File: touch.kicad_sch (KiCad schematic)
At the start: 4 parts, among them J3 Touch_Top, J4 Touch_Top, U7 MTCH2120-V/REB, U8 MTCH2120-V/REB

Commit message: save progress before refactor
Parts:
- added R13, R14, R15, R16, R17, R18, R19, R20, R21, R22, R23, R24, R25, R26, R27, R28, R29, R30, R31, R32, R33, R34, R35, R36: 100k, Resistor_SMD:R_0402_1005Metric, symbol Device:R_Small
- J3: now left out of the parts list
- J4: value Touch_Top -> Touch_Btm; now left out of the parts list
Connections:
- net at U8.10 (BUTTON5/GPIO5): now also R18.2
- net at U8.13 (BUTTON6/GPIO6): now also R19.1
- net at U8.14 (BUTTON7/GPIO7): now also R20.1
- net at U8.15 (BUTTON8/GPIO8): now also R21.1
- net at U8.16 (BUTTON9/GPIO9): now also R22.1
- net at U8.17 (BUTTON10/GPIO10): now also R23.1
- net at U8.18 (BUTTON11/DS/GPIO11): now also R24.1
- net at U8.5 (BUTTON0/GPIO0): now also R13.2
- net at U8.6 (BUTTON1/GPIO1): now also R14.2
- net at U8.7 (BUTTON2/GPIO2): now also R15.2
- net at U8.8 (BUTTON3/GPIO3): now also R16.2
- net at U8.9 (BUTTON4/GPIO4): now also R17.2
- net TOUCH_BTM_1: now reaches J4.1 (Pin_1)
- net TOUCH_BTM_1: now also R13.1
- net TOUCH_BTM_10: now reaches J4.10 (Pin_10)
- net TOUCH_BTM_10: now also R22.2
- net TOUCH_BTM_11: now reaches J4.11 (Pin_11)
- net TOUCH_BTM_11: now also R23.2
- net TOUCH_BTM_12: now reaches J4.12 (Pin_12)
- net TOUCH_BTM_12: now also R24.2
- net TOUCH_BTM_2: now reaches J4.2 (Pin_2)
- net TOUCH_BTM_2: now also R14.1
- net TOUCH_BTM_3: now reaches J4.3 (Pin_3)
- net TOUCH_BTM_3: now also R15.1
- net TOUCH_BTM_4: now reaches J4.4 (Pin_4)
- net TOUCH_BTM_4: now also R16.1
- net TOUCH_BTM_5: now reaches J4.5 (Pin_5)
- net TOUCH_BTM_5: now also R17.1
- net TOUCH_BTM_6: now reaches J4.6 (Pin_6)
- net TOUCH_BTM_6: now also R18.1
- net TOUCH_BTM_7: now reaches J4.7 (Pin_7)
- net TOUCH_BTM_7: now also R19.2
- net TOUCH_BTM_8: now reaches J4.8 (Pin_8)
- net TOUCH_BTM_8: now also R20.2
- net TOUCH_BTM_9: now reaches J4.9 (Pin_9)
- net TOUCH_BTM_9: now also R21.2
- net at U7.10 (BUTTON5/GPIO5): now also R30.2
- net at U7.13 (BUTTON6/GPIO6): now also R36.1
- net at U7.14 (BUTTON7/GPIO7): now also R35.1
- net at U7.15 (BUTTON8/GPIO8): now also R34.1
- net at U7.16 (BUTTON9/GPIO9): now also R33.1
- net at U7.17 (BUTTON10/GPIO10): now also R32.1
- net at U7.18 (BUTTON11/DS/GPIO11): now also R31.1
- net GND: now reaches U7.2 (ADD_SEL)
- net at U7.5 (BUTTON0/GPIO0): now also R25.2
- net at U7.6 (BUTTON1/GPIO1): now also R26.2
- net at U7.7 (BUTTON2/GPIO2): now also R27.2
- net at U7.8 (BUTTON3/GPIO3): now also R28.2
- net at U7.9 (BUTTON4/GPIO4): now also R29.2
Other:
- moved on the sheet: J4

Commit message: progress dump
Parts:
- added C35, C37: 100nF, symbol Device:C_Small
- added C36, C38: 2.2uF, symbol Device:C_Small
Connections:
- net GND: now also U7.12 (GPIO12), U7.21 (EPAD), U7.3 (GND), U8.12 (GPIO12), U8.21 (EPAD), U8.3 (GND), C35.2, C36.2, C37.2, C38.2
- net TOUCH_TOP_4: now reaches R28.1
- net TOUCH_TOP_4: now also J3.4 (Pin_4)
- net TOUCH_TOP_3: now reaches R27.1
- net TOUCH_TOP_3: now also J3.3 (Pin_3)
- net SCL_G1: now reaches U8.1 (SCL)
- net SCL_G1: now also U7.1 (SCL)
- net TOUCH_INT: now reaches U8.11 (INT*)
- net TOUCH_INT: now also U7.11 (INT*)
- net TOUCH_RST: now reaches U8.19 (RESET*)
- net TOUCH_RST: now also U7.19 (RESET*)
- net +3V3_G1: now reaches U8.2 (ADD_SEL)
- net +3V3_G1: now also U7.4 (VDD), U8.4 (VDD), C35.1, C36.1, C37.1, C38.1
- net SDA_G1: now reaches U8.20 (SDA)
- net SDA_G1: now also U7.20 (SDA)
- net TOUCH_TOP_6: now reaches R30.1
- net TOUCH_TOP_6: now also J3.6 (Pin_6)
- net TOUCH_TOP_8: now reaches R35.2
- net TOUCH_TOP_8: now also J3.8 (Pin_8)
- net TOUCH_TOP_1: now reaches J3.1 (Pin_1)
- net TOUCH_TOP_1: now also R25.1
- net TOUCH_TOP_10: now reaches J3.10 (Pin_10)
- net TOUCH_TOP_10: now also R33.2
- net TOUCH_TOP_11: now reaches J3.11 (Pin_11)
- net TOUCH_TOP_11: now also R32.2
- net TOUCH_TOP_12: now reaches J3.12 (Pin_12)
- net TOUCH_TOP_12: now also R31.2
- net TOUCH_TOP_2: now reaches J3.2 (Pin_2)
- net TOUCH_TOP_2: now also R26.1
- net TOUCH_TOP_5: now reaches J3.5 (Pin_5)
- net TOUCH_TOP_5: now also R29.1
- net TOUCH_TOP_7: now reaches J3.7 (Pin_7)
- net TOUCH_TOP_7: now also R36.2
- net TOUCH_TOP_9: now reaches J3.9 (Pin_9)
- net TOUCH_TOP_9: now also R34.2
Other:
- moved on the sheet: J3

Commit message: finish up everything but nfc
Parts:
- C35, C37: footprint (none) -> Capacitor_SMD:C_0402_1005Metric; LCSC Part (none) -> C1525
- C36, C38: footprint (none) -> Capacitor_SMD:C_0402_1005Metric; LCSC Part (none) -> C12530
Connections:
- net +3V3_G1 renamed +3V3_G2
- net SCL_G1 renamed SCL_G2
- net SDA_G1 renamed SDA_G2

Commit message: progress
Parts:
- removed J3: Touch_Top, custom_footprints:Touch_Surface_12_Pad, symbol Connector_Generic:Conn_01x12
- removed J4: Touch_Btm, custom_footprints:Touch_Surface_12_Pad, symbol Connector_Generic:Conn_01x12
- removed R15, R16, R17, R18, R19, R20, R21, R22, R23, R24, R25, R26, R27, R28, R29, R30, R31, R32, R33, R34, R35, R36: 100k, Resistor_SMD:R_0402_1005Metric, symbol Device:R_Small
- removed U7, U8: MTCH2120-V/REB, MTCH2120:QFN_MTCH2120-V&slash_REB_MCH, symbol MTCH2120:MTCH2120-V_REB
- added R10, R9: 4.7k, symbol Device:R_Small
- added U7, U8: CAP1208-1-A4-TR, QFN16_3x3MC_MCH, symbol CAP1208-1-A4-TR:CAP1208-1-A4-TR
- C35, C37: footprint Capacitor_SMD:C_0402_1005Metric -> (none); LCSC Part C1525 -> (none)
- C36, C38: value 2.2uF -> 1uF; footprint Capacitor_SMD:C_0402_1005Metric -> (none); LCSC Part C12530 -> (none)
- R13, R14: value 100k -> 4.7k; footprint Resistor_SMD:R_0402_1005Metric -> (none); LCSC Part C25741 -> (none)
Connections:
- net TOUCH_BTM_1 is gone; now on net +3V3_G2: R13.1
- net TOUCH_BTM_2 is gone; now on net +3V3_G2: R14.1
- net +3V3_G2: now also R10.1, R9.1, U7.4 (VDD), U8.4 (VDD)
- net GND: now also U7.17 (EPAD), U7.7 (GND), U7.8 (GND), U8.17 (EPAD), U8.7 (GND), U8.8 (GND)
- net TOUCH_INT: now also U7.1 (*ALERT), U8.1 (*ALERT)
- net SDA_T2: now reaches R13.2
- net SDA_T2: now also U8.2 (SMDATA)
- net SCL_T2: now reaches R14.2
- net SCL_T2: now also U8.3 (SMCLK)
- new net SCL_T1: R10.2, U7.3 (SMCLK)
- new net SDA_T1: R9.2, U7.2 (SMDATA)

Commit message: push changes before removing fuel gauge
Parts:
- added J3: Touch_Surface_Top, custom_footprints:Touch_Surface_8_Pad, symbol Connector_Generic:Conn_01x08
- added J4: Touch_Surface_Bottom, custom_footprints:Touch_Surface_8_Pad, symbol Connector_Generic:Conn_01x08
- C35, C37: footprint (none) -> Capacitor_SMD:C_0402_1005Metric; LCSC Part (none) -> C1525
- C36, C38: footprint (none) -> Capacitor_SMD:C_0402_1005Metric; LCSC Part (none) -> C52923
- R10, R13, R14, R9: footprint (none) -> Resistor_SMD:R_0402_1005Metric; LCSC Part (none) -> C25900
- U7, U8: LCSC Part (none) -> C2652055; now left out of the parts list
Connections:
- net at U7.10 (CS7): now also J3.7 (Pin_7)
- net at U7.11 (CS6): now also J3.6 (Pin_6)
- net at U7.12 (CS5): now also J3.5 (Pin_5)
- net at U7.13 (CS4): now also J3.4 (Pin_4)
- net at U7.14 (CS3): now also J3.3 (Pin_3)
- net at U7.15 (CS2): now also J3.2 (Pin_2)
- net at U7.16 (CS1): now also J3.1 (Pin_1)
- net at U7.9 (CS8): now also J3.8 (Pin_8)
- net at U8.10 (CS7): now also J4.7 (Pin_7)
- net at U8.11 (CS6): now also J4.6 (Pin_6)
- net at U8.12 (CS5): now also J4.5 (Pin_5)
- net at U8.13 (CS4): now also J4.4 (Pin_4)
- net at U8.14 (CS3): now also J4.3 (Pin_3)
- net at U8.15 (CS2): now also J4.2 (Pin_2)
- net at U8.16 (CS1): now also J4.1 (Pin_1)
- net at U8.9 (CS8): now also J4.8 (Pin_8)

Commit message: hopefully final schematic before splitting out
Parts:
- J3, J4: now left out of the parts list
- U6: renamed from U7; now in the parts list
- U7: renamed from U8; now in the parts list
- renumbered C35 to C22, C37 to C23, C36 to C24, C38 to C25, R9 to R10, R13 to R11, R10 to R12, R14 to R13
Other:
- moved on the sheet: C22, C23, C24, C25, J3, J4, R10, R11, R12, R13, U6, U7

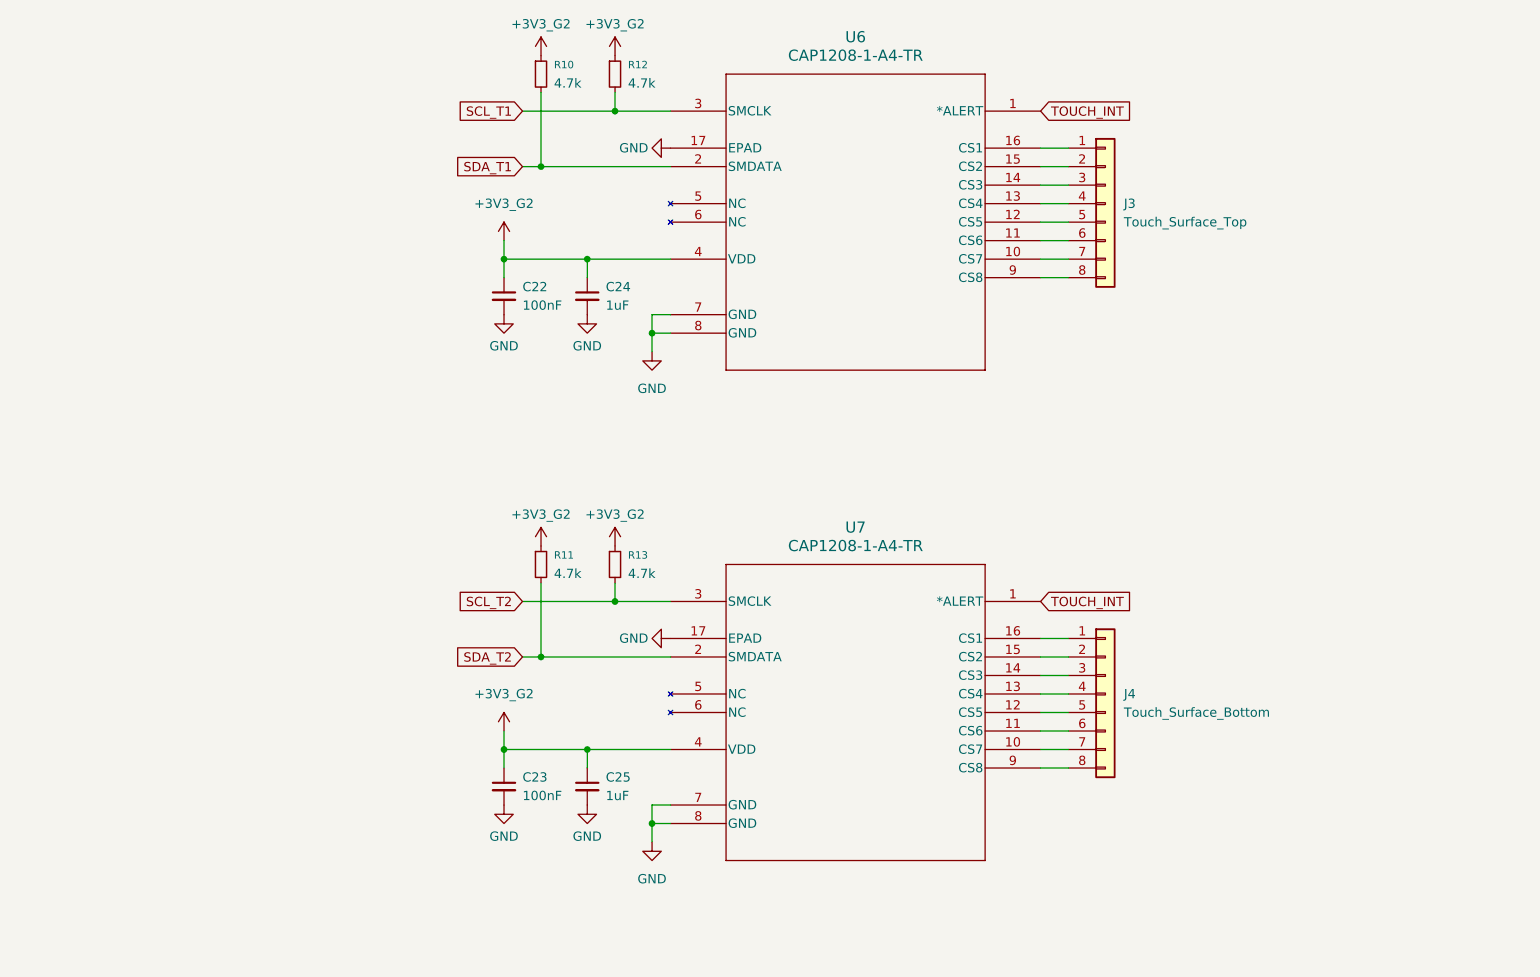
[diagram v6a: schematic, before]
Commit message: prepare schematic for devboard
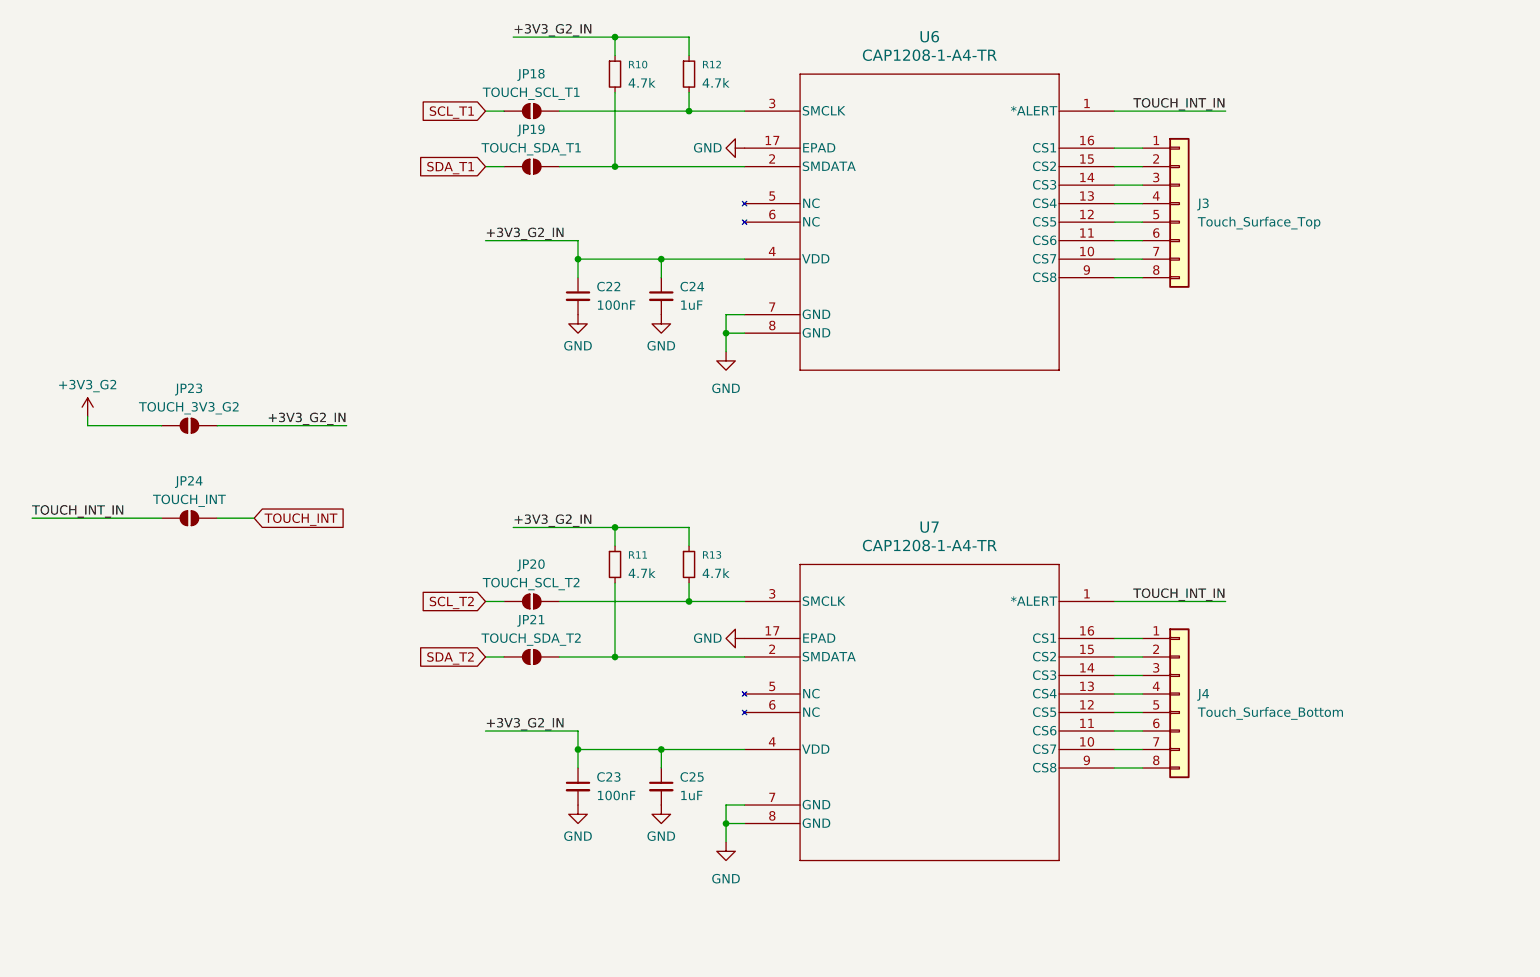
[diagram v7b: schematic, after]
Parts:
- added JP18: TOUCH_SCL_T1, Jumper:SolderJumper-2_P1.3mm_Open_Pad1.0x1.5mm, symbol Jumper:SolderJumper_2_Open
- added JP19: TOUCH_SDA_T1, Jumper:SolderJumper-2_P1.3mm_Open_Pad1.0x1.5mm, symbol Jumper:SolderJumper_2_Open
- added JP20: TOUCH_SCL_T2, Jumper:SolderJumper-2_P1.3mm_Open_Pad1.0x1.5mm, symbol Jumper:SolderJumper_2_Open
- added JP21: TOUCH_SDA_T2, Jumper:SolderJumper-2_P1.3mm_Open_Pad1.0x1.5mm, symbol Jumper:SolderJumper_2_Open
- added JP23: TOUCH_3V3_G2, Jumper:SolderJumper-2_P1.3mm_Open_Pad1.0x1.5mm, symbol Jumper:SolderJumper_2_Open
- added JP24: TOUCH_INT, Jumper:SolderJumper-2_P1.3mm_Open_Pad1.0x1.5mm, symbol Jumper:SolderJumper_2_Open
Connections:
- net +3V3_G2: now also JP23.1 (A); no longer C22.1, C23.1, C24.1, C25.1, R10.1, R11.1, R12.1, R13.1, U6.4 (VDD), U7.4 (VDD)
- net SCL_T1: now also JP18.1 (A); no longer R12.2, U6.3 (SMCLK)
- net SCL_T2: now also JP20.1 (A); no longer R13.2, U7.3 (SMCLK)
- net SDA_T1: now also JP19.1 (A); no longer R10.2, U6.2 (SMDATA)
- net SDA_T2: now also JP21.1 (A); no longer R11.2, U7.2 (SMDATA)
- net TOUCH_INT: now also JP24.2 (B); no longer U6.1 (*ALERT), U7.1 (*ALERT)
- new net: JP21.2 (B), R11.2, U7.2 (SMDATA)
- new net: JP19.2 (B), R10.2, U6.2 (SMDATA)
- new net: JP18.2 (B), R12.2, U6.3 (SMCLK)
- new net: JP20.2 (B), R13.2, U7.3 (SMCLK)
- new net +3V3_G2_IN: C22.1, C23.1, C24.1, C25.1, JP23.2 (B), R10.1, R11.1, R12.1, R13.1, U6.4 (VDD), U7.4 (VDD)
- new net TOUCH_INT_IN: JP24.1 (A), U6.1 (*ALERT), U7.1 (*ALERT)
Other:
- moved on the sheet: C22, C23, C24, C25, J3, J4, R10, R11, R12, R13, U6, U7

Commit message: huge progress on bentoboard, schematic fixes
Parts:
- added R3: 100k, Resistor_SMD:R_0402_1005Metric, symbol Device:R_Small
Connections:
- net +3V3_G2_IN: now also R3.2
- net TOUCH_INT_IN: now also R3.1
- net at U7.10 (CS7): now also J4.2 (Pin_2); no longer J4.7 (Pin_7)
- net at U7.11 (CS6): now also J4.3 (Pin_3); no longer J4.6 (Pin_6)
- net at U7.12 (CS5): now also J4.4 (Pin_4); no longer J4.5 (Pin_5)
- net at U7.13 (CS4): now also J4.5 (Pin_5); no longer J4.4 (Pin_4)
- net at U7.14 (CS3): now also J4.6 (Pin_6); no longer J4.3 (Pin_3)
- net at U7.15 (CS2): now also J4.7 (Pin_7); no longer J4.2 (Pin_2)
- net at U7.16 (CS1): now also J4.8 (Pin_8); no longer J4.1 (Pin_1)
- net at U7.9 (CS8): now also J4.1 (Pin_1); no longer J4.8 (Pin_8)
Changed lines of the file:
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@@
+	(wire
+		(pts
+			(xy 60.96 125.73) (xy 57.15 125.73)
+		)
+		(stroke
+			(width 0)
+			(type default)
+		)
+	)
 	(wire
 		(pts
@@
 	(wire
 		(pts
+			(xy 60.96 123.19) (xy 60.96 125.73)
+		)
+		(stroke
+			(width 0)
+			(type default)
+		)
+	)
+	(wire
+		(pts
 			(xy 109.22 129.54) (xy 116.84 129.54)
 		)
@@
 	(wire
 		(pts
+			(xy 60.96 123.19) (xy 72.39 123.19)
+		)
+		(stroke
+			(width 0)
+			(type default)
+		)
+	)
+	(wire
+		(pts
 			(xy 185.42 62.23) (xy 189.23 62.23)
 		)
@@
 	(wire
 		(pts
+			(xy 35.56 125.73) (xy 52.07 125.73)
+		)
+		(stroke
+			(width 0)
+			(type default)
+		)
+	)
+	(wire
+		(pts
 			(xy 111.76 77.47) (xy 111.76 74.93)
 		)
@@
 			(width 0)
 			(type default)
+		)
+	)
+	(label "+3V3_G2_IN"
+		(at 72.39 123.19 180)
+		(effects
+			(font
+				(size 1.27 1.27)
+			)
+			(justify right bottom)
 		)
 	)
 	(label "+3V3_G2_IN"
 		(at 99.06 72.39 0)
+		(effects
+			(font
+				(size 1.27 1.27)
+			)
+			(justify left bottom)
+		)
+	)
+	(label "TOUCH_INT_IN"
+		(at 35.56 125.73 0)
 		(effects
 			(font
@@
 	)
 	(symbol
+		(lib_id "Device:R_Small")
+		(at 54.61 125.73 90)
+		(unit 1)
+		(exclude_from_sim no)
+		(in_bom yes)
+		(on_board yes)
+		(dnp no)
+		(property "Reference" "R3"
+			(at 54.61 122.174 90)
+			(effects
+				(font
+					(size 1.016 1.016)
+				)
+			)
+		)
+		(property "Value" "100k"
+			(at 54.61 123.952 90)
+			(effects
+				(font
+					(size 1.27 1.27)
+				)
+			)
+		)
+		(property "Footprint" "Resistor_SMD:R_0402_1005Metric"
+			(at 54.61 125.73 0)
+			(effects
+				(font
+					(size 1.27 1.27)
+				)
+				(hide yes)
+			)
+		)
+		(property "Datasheet" "~"
+			(at 54.61 125.73 0)
+			(effects
+				(font
+					(size 1.27 1.27)
+				)
+				(hide yes)
+			)
+		)
+		(property "Description" "Resistor, small symbol"
+			(at 54.61 125.73 0)
+			(effects
+				(font
+					(size 1.27 1.27)
+				)
+				(hide yes)
+			)
+		)
+		(property "LCSC Part" "C25741"
+			(at 54.61 125.73 90)
+			(effects
+				(font
+					(size 1.27 1.27)
+				)
+				(hide yes)
+			)
+		)
+		(property "CREATOR" ""
+			(at 54.61 125.73 90)
+			(effects
+				(font
+					(size 1.27 1.27)
+				)
+				(hide yes)
+			)
+		)
+		(property "MAXIMUM_PACKAGE_HEIGHT" ""
+			(at 54.61 125.73 90)
+			(effects
+				(font
+					(size 1.27 1.27)
+				)
+				(hide yes)
+			)
+		)
+		(property "PARTREV" ""
+			(at 54.61 125.73 90)
+			(effects
+				(font
+					(size 1.27 1.27)
+				)
+				(hide yes)
+			)
+		)
+		(property "VERIFIER" ""
+			(at 54.61 125.73 90)
+			(effects
+				(font
+					(size 1.27 1.27)
+				)
+				(hide yes)
+			)
+		)
+		(pin "2"
+		)
+		(pin "1"
+		)
+		(instances
+			(project "rc_keychain"
+				(path "/c6cb5a1d-9f97-4766-8582-a9e93ed049e4/7b6f6d0f-0137-41ad-b85b-11085abf19c4"
+					(reference "R3")
+					(unit 1)
+				)
+			)
+		)
+	)
+	(symbol
 		(lib_id "Jumper:SolderJumper_2_Open")
 		(at 105.41 121.92 0)
@@
 	(symbol
 		(lib_id "Connector_Generic:Conn_01x08")
-		(at 194.31 134.62 0)
+		(at 194.31 137.16 0)
+		(mirror x)
 		(unit 1)
 		(exclude_from_sim no)
@@
 		(on_board yes)
 		(dnp no)
-		(fields_autoplaced yes)
 		(property "Reference" "J4"
-			(at 196.85 134.6199 0)
+			(at 196.85 137.1601 0)
 			(effects
 				(font
@@
 		)
 		(property "Value" "Touch_Surface_Bottom"
-			(at 196.85 137.1599 0)
+			(at 196.85 134.6201 0)
 			(effects
 				(font
@@
 		)
 		(property "Footprint" "custom_footprints:Touch_Surface_8_Pad"
-			(at 194.31 134.62 0)
+			(at 194.31 137.16 0)
 			(effects
 				(font
@@
 		)
 		(property "Datasheet" "~"
-			(at 194.31 134.62 0)
+			(at 194.31 137.16 0)
 			(effects
 				(font
@@
 		)
 		(property "Description" "Generic connector, single row, 01x08, script generated (kicad-library-utils/schlib/autogen/connector/)"
-			(at 194.31 134.62 0)
-			(effects
-				(font
+			(at 194.31 137.16 0)
+			(effects
+				(font
